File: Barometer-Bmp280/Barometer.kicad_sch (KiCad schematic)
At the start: 3 parts, among them U44 BMP280

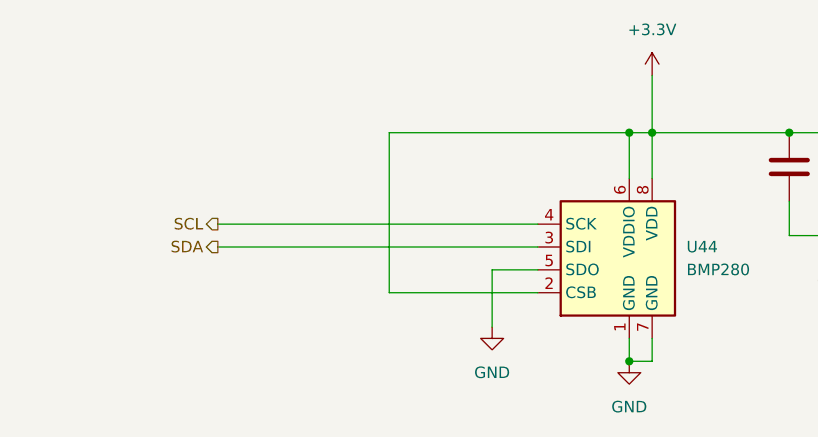
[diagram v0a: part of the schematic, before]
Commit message: Route sensors, IMU and radio board
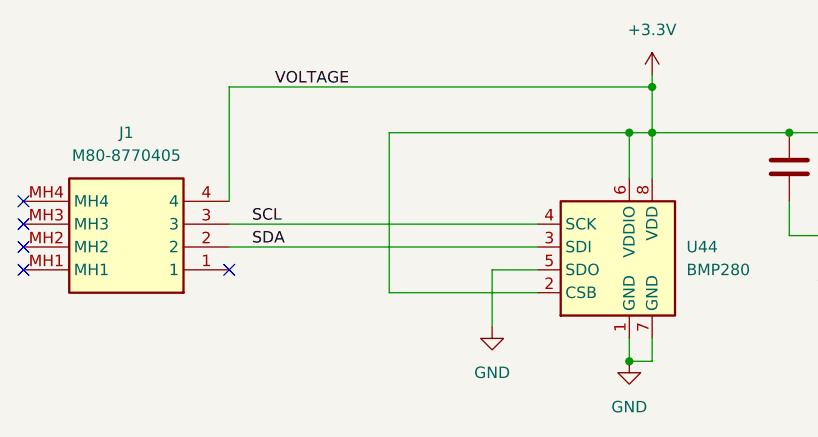
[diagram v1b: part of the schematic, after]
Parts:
- added J1: M80-8770405, M808770405, symbol M80-8770405:M80-8770405
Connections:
- net +3.3V: now also J1.4
- net SCL: now also J1.3
- net SDA: now also J1.2
- no-connect marks 0 -> 5
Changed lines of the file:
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@@
   (junction (at 173.99 96.52) (diameter 0) (color 0 0 0 0)
   )
+  (junction (at 158.75 91.44) (diameter 0) (color 0 0 0 0)
+  )
   (junction (at 179.07 107.95) (diameter 0) (color 0 0 0 0)
   )
@@
   (junction (at 158.75 96.52) (diameter 0) (color 0 0 0 0)
   )
-  (wire (pts (xy 110.49 109.22) (xy 146.05 109.22))
+  (no_connect (at 88.9 104.14))
+  (no_connect (at 111.76 111.76))
+  (no_connect (at 88.9 109.22))
+  (no_connect (at 88.9 106.68))
+  (no_connect (at 88.9 111.76))
+  (wire (pts (xy 111.76 91.44) (xy 158.75 91.44))
     (stroke (width 0) (type default))
   )
@@
     (stroke (width 0) (type default))
   )
+  (wire (pts (xy 111.76 109.22) (xy 146.05 109.22))
+    (stroke (width 0) (type default))
+  )
   (wire (pts (xy 179.07 107.95) (xy 186.69 107.95))
     (stroke (width 0) (type default))
@@
     (stroke (width 0) (type default))
   )
-  (wire (pts (xy 110.49 106.68) (xy 146.05 106.68))
-    (stroke (width 0) (type default))
-  )
   (wire (pts (xy 129.54 96.52) (xy 156.21 96.52))
     (stroke (width 0) (type default))
@@
     (stroke (width 0) (type default))
   )
+  (wire (pts (xy 111.76 106.68) (xy 146.05 106.68))
+    (stroke (width 0) (type default))
+  )
   (wire (pts (xy 186.69 107.95) (xy 186.69 104.14))
     (stroke (width 0) (type default))
@@
     (stroke (width 0) (type default))
   )
-  (wire (pts (xy 158.75 90.17) (xy 158.75 96.52))
+  (wire (pts (xy 158.75 90.17) (xy 158.75 91.44))
     (stroke (width 0) (type default))
   )
@@
     (stroke (width 0) (type default))
   )
-  (hierarchical_label "SDA" (shape output) (at 110.49 109.22 180) (fields_autoplaced)
-    (effects (font (size 1.27 1.27)) (justify right))
-  )
-  (hierarchical_label "SCL" (shape output) (at 110.49 106.68 180) (fields_autoplaced)
-    (effects (font (size 1.27 1.27)) (justify right))
+  (wire (pts (xy 158.75 91.44) (xy 158.75 96.52))
+    (stroke (width 0) (type default))
+  )
+  (wire (pts (xy 111.76 104.14) (xy 111.76 91.44))
+    (stroke (width 0) (type default))
+  )
+  (label "SCL" (at 114.3 106.68 0) (fields_autoplaced)
+    (effects (font (size 1.27 1.27)) (justify left bottom))
+  )
+  (label "SDA" (at 114.3 109.22 0) (fields_autoplaced)
+    (effects (font (size 1.27 1.27)) (justify left bottom))
+  )
+  (label "VOLTAGE" (at 116.84 91.44 0) (fields_autoplaced)
+    (effects (font (size 1.27 1.27)) (justify left bottom))
   )
   (symbol (lib_id "Device:C") (at 186.69 100.33 0) (unit 1)
@@
         )
       )
+    )
+  )
+  (symbol (lib_id "M80-8770405:M80-8770405") (at 111.76 111.76 180) (unit 1)
+    (in_bom yes) (on_board yes) (dnp no) (fields_autoplaced)
+    (property "Reference" "J1" (at 100.33 96.52 0)
+      (effects (font (size 1.27 1.27)))
+    )
+    (property "Value" "M80-8770405" (at 100.33 99.06 0)
+      (effects (font (size 1.27 1.27)))
+    )
+    (property "Footprint" "M808770405" (at 92.71 16.84 0)
+      (effects (font (size 1.27 1.27)) (justify left top) hide)
+    )
+    (property "Datasheet" "https://cdn.harwin.com/pdfs/M80-877.pdf" (at 92.71 -83.16 0)
+      (effects (font (size 1.27 1.27)) (justify left top) hide)
+    )
+    (property "Height" "5.56" (at 92.71 -283.16 0)
+      (effects (font (size 1.27 1.27)) (justify left top) hide)
+    )
+    (property "Manufacturer_Name" "Harwin" (at 92.71 -383.16 0)
+      (effects (font (size 1.27 1.27)) (justify left top) hide)
+    )
+    (property "Manufacturer_Part_Number" "M80-8770405" (at 92.71 -483.16 0)
+      (effects (font (size 1.27 1.27)) (justify left top) hide)
+    )
+    (property "Mouser Part Number" "855-M80-8770405" (at 92.71 -583.16 0)
+      (effects (font (size 1.27 1.27)) (justify left top) hide)
+    )
+    (property "Mouser Price/Stock" "https://www.mouser.co.uk/ProductDetail/Harwin/M80-8770405?qs=3tymCvhQ29ZPq83M%252Bf8kIA%3D%3D" (at 92.71 -683.16 0)
+      (effects (font (size 1.27 1.27)) (justify left top) hide)
+    )
+    (property "Arrow Part Number" "" (at 92.71 -783.16 0)
+      (effects (font (size 1.27 1.27)) (justify left top) hide)
+    )
+    (property "Arrow Price/Stock" "" (at 92.71 -883.16 0)
+      (effects (font (size 1.27 1.27)) (justify left top) hide)
+    )
+    (pin "1")
+    (pin "2")
+    (pin "3")
+    (pin "4")
+    (pin "MH1")
+    (pin "MH2")
+    (pin "MH3")
+    (pin "MH4")
+    (instances
+      (project "Barometer"
+        (path "/7f3991ce-16d8-4280-80b6-77a7b05059d0"
+          (reference "J1") (unit 1)
+        )
+      )

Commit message: Done with most of the boards
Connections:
- net GND: now also J1.1
- no-connect marks 5 -> 4
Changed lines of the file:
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@@
   (junction (at 156.21 121.92) (diameter 0) (color 0 0 0 0)
+  )
+  (junction (at 140.97 116.84) (diameter 0) (color 0 0 0 0)
   )
   (junction (at 158.75 96.52) (diameter 0) (color 0 0 0 0)
   )
   (no_connect (at 88.9 104.14))
-  (no_connect (at 111.76 111.76))
   (no_connect (at 88.9 109.22))
   (no_connect (at 88.9 106.68))
@@
   )
   (wire (pts (xy 173.99 96.52) (xy 186.69 96.52))
+    (stroke (width 0) (type default))
+  )
+  (wire (pts (xy 123.19 111.76) (xy 123.19 116.84))
     (stroke (width 0) (type default))
   )
@@
     (stroke (width 0) (type default))
   )
+  (wire (pts (xy 111.76 111.76) (xy 123.19 111.76))
+    (stroke (width 0) (type default))
+  )
   (wire (pts (xy 111.76 109.22) (xy 146.05 109.22))
     (stroke (width 0) (type default))
@@
     (stroke (width 0) (type default))
   )
+  (wire (pts (xy 123.19 116.84) (xy 140.97 116.84))
+    (stroke (width 0) (type default))
+  )
   (wire (pts (xy 129.54 114.3) (xy 129.54 96.52))
+    (stroke (width 0) (type default))
+  )
+  (wire (pts (xy 140.97 116.84) (xy 140.97 118.11))
     (stroke (width 0) (type default))
   )
@@
     (stroke (width 0) (type default))
   )
-  (wire (pts (xy 140.97 111.76) (xy 140.97 118.11))
+  (wire (pts (xy 140.97 111.76) (xy 140.97 116.84))
     (stroke (width 0) (type default))
   )

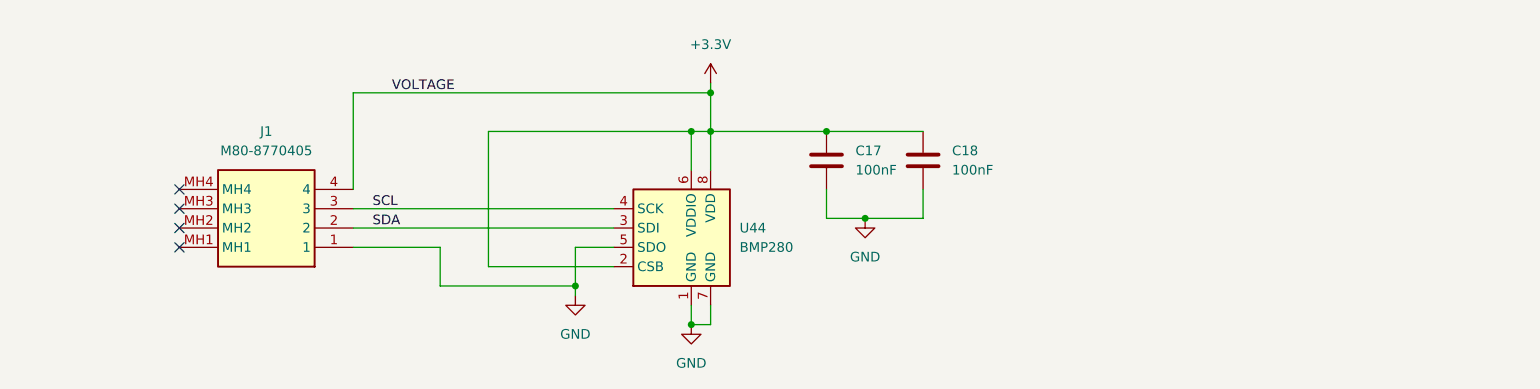
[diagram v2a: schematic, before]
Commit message: Fixed Accel, Barometer, FRAM, Inertia unit, and Magnetometer
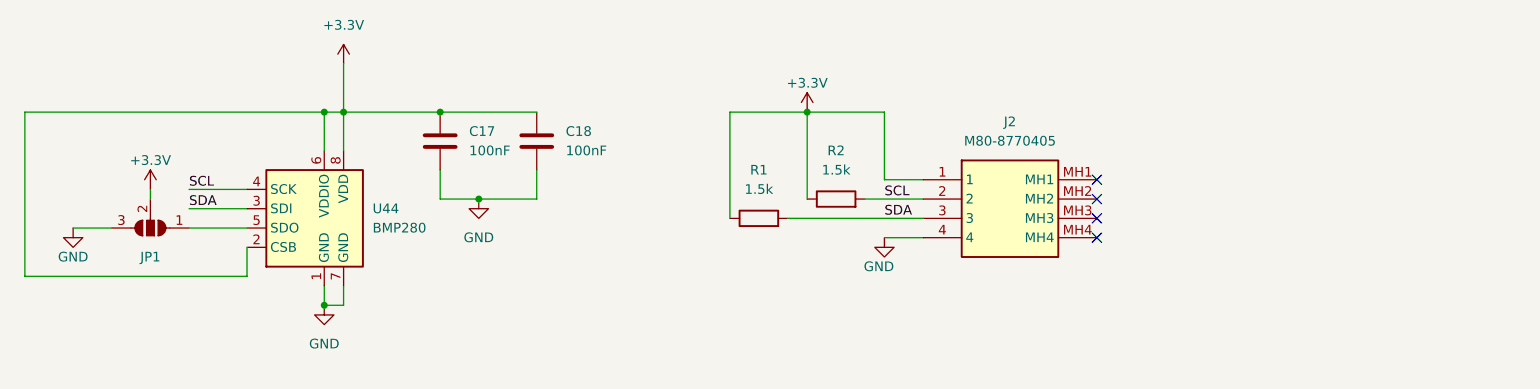
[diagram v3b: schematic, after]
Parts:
- removed J1: M80-8770405, M808770405, symbol M80-8770405:M80-8770405
- added J2: M80-8770405, M808770405, symbol M80-8770405:M80-8770405
- added JP1: SolderJumper_3_Open, Jumper:SolderJumper-3_P1.3mm_Open_RoundedPad1.0x1.5mm_NumberLabels, symbol Jumper:SolderJumper_3_Open
- added R1, R2: 1.5k, Resistor_SMD:R_0201_0603Metric_Pad0.64x0.40mm_HandSolder, symbol Device:R
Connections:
- net +3.3V: now also J2.1, JP1.2 (C), R1.1, R2.1
- net GND: now also J2.4, JP1.3 (B); no longer U44.5 (SDO)
- net SCL: now also J2.2, R2.2
- net SDA: now also J2.3, R1.2
- new net: JP1.1 (A), U44.5 (SDO)
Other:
- company: (none) -> USST Avionics
- title: (none) -> BMP280 Barometer
- moved on the sheet: C17, C18, U44

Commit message: Started fixing layouts
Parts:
- renumbered J2 to J1
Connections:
- net +3.3V: now also JP1.3 (B); no longer JP1.2 (C)
- net GND: now also JP1.1 (A); no longer JP1.3 (B)
- net at U44.5 (SDO): now also JP1.2 (C); no longer JP1.1 (A)
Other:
- moved on the sheet: JP1
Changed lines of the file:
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@@
     (stroke (width 0) (type default))
   )
-  (wire (pts (xy 97.79 115.57) (xy 68.58 115.57))
+  (wire (pts (xy 97.79 120.65) (xy 67.31 120.65))
     (stroke (width 0) (type default))
   )
@@
     (stroke (width 0) (type default))
   )
-  (wire (pts (xy 90.17 109.22) (xy 97.79 109.22))
+  (wire (pts (xy 85.09 114.3) (xy 85.09 115.57))
+    (stroke (width 0) (type default))
+  )
+  (wire (pts (xy 97.79 111.76) (xy 97.79 120.65))
+    (stroke (width 0) (type default))
+  )
+  (wire (pts (xy 85.09 102.87) (xy 85.09 104.14))
+    (stroke (width 0) (type default))
+  )
+  (wire (pts (xy 88.9 109.22) (xy 97.79 109.22))
     (stroke (width 0) (type default))
   )
@@
     (stroke (width 0) (type default))
   )
-  (wire (pts (xy 85.09 104.14) (xy 85.09 105.41))
-    (stroke (width 0) (type default))
-  )
   (wire (pts (xy 107.95 93.98) (xy 110.49 93.98))
     (stroke (width 0) (type default))
@@
     (stroke (width 0) (type default))
   )
-  (wire (pts (xy 97.79 115.57) (xy 97.79 111.76))
-    (stroke (width 0) (type default))
-  )
   (wire (pts (xy 168.91 107.95) (xy 186.69 107.95))
     (stroke (width 0) (type default))
@@
     (stroke (width 0) (type default))
   )
-  (wire (pts (xy 74.93 109.22) (xy 80.01 109.22))
-    (stroke (width 0) (type default))
-  )
   (wire (pts (xy 110.49 116.84) (xy 110.49 119.38))
     (stroke (width 0) (type default))
   )
-  (wire (pts (xy 68.58 93.98) (xy 107.95 93.98))
+  (wire (pts (xy 67.31 93.98) (xy 107.95 93.98))
     (stroke (width 0) (type default))
   )
@@
     (stroke (width 0) (type default))
   )
-  (wire (pts (xy 68.58 115.57) (xy 68.58 93.98))
+  (wire (pts (xy 67.31 120.65) (xy 67.31 93.98))
     (stroke (width 0) (type default))
   )
@@
     )
   )
-  (symbol (lib_id "Jumper:SolderJumper_3_Open") (at 85.09 109.22 180) (unit 1)
-    (in_bom yes) (on_board yes) (dnp no) (fields_autoplaced)
-    (property "Reference" "JP1" (at 85.09 113.03 0)
-      (effects (font (size 1.27 1.27)))
-    )
-    (property "Value" "SolderJumper_3_Open" (at 85.09 115.57 0)
+  (symbol (lib_id "Jumper:SolderJumper_3_Open") (at 85.09 109.22 90) (unit 1)
+    (in_bom yes) (on_board yes) (dnp no)
+    (property "Reference" "JP1" (at 88.9 115.57 90)
+      (effects (font (size 1.27 1.27)) (justify left))
+    )
+    (property "Value" "SolderJumper_3_Open" (at 78.74 109.22 0)
       (effects (font (size 1.27 1.27)) hide)
     )
@@
     )
   )
-  (symbol (lib_id "power:+3.3V") (at 85.09 104.14 0) (unit 1)
-    (in_bom yes) (on_board yes) (dnp no)
-    (property "Reference" "#PWR019" (at 85.09 107.95 0)
-      (effects (font (size 1.27 1.27)) hide)
-    )
-    (property "Value" "+3.3V" (at 85.09 100.33 0)
-      (effects (font (size 1.27 1.27)))
-    )
-    (property "Footprint" "" (at 85.09 104.14 0)
-      (effects (font (size 1.27 1.27)) hide)
-    )
-    (property "Datasheet" "" (at 85.09 104.14 0)
+  (symbol (lib_id "power:+3.3V") (at 85.09 102.87 0) (unit 1)
+    (in_bom yes) (on_board yes) (dnp no)
+    (property "Reference" "#PWR019" (at 85.09 106.68 0)
+      (effects (font (size 1.27 1.27)) hide)
+    )
+    (property "Value" "+3.3V" (at 85.09 99.06 0)
+      (effects (font (size 1.27 1.27)))
+    )
+    (property "Footprint" "" (at 85.09 102.87 0)
+      (effects (font (size 1.27 1.27)) hide)
+    )
+    (property "Datasheet" "" (at 85.09 102.87 0)
       (effects (font (size 1.27 1.27)) hide)
     )
@@
   (symbol (lib_id "M80-8770405:M80-8770405") (at 186.69 102.87 0) (unit 1)
     (in_bom yes) (on_board yes) (dnp no)
-    (property "Reference" "J2" (at 198.12 95.25 0)
+    (property "Reference" "J1" (at 198.12 95.25 0)
       (effects (font (size 1.27 1.27)))
     )
@@
       (project "Barometer"
         (path "/7f3991ce-16d8-4280-80b6-77a7b05059d0"
-          (reference "J2") (unit 1)
+          (reference "J1") (unit 1)
         )
       )
@@
     )
   )
-  (symbol (lib_id "power:GND") (at 74.93 109.22 0) (unit 1)
-    (in_bom yes) (on_board yes) (dnp no)
-    (property "Reference" "#PWR03" (at 74.93 115.57 0)
-      (effects (font (size 1.27 1.27)) hide)
-    )
-    (property "Value" "GND" (at 74.93 113.03 0)
-      (effects (font (size 1.27 1.27)))
-    )
-    (property "Footprint" "" (at 74.93 109.22 0)
-      (effects (font (size 1.27 1.27)) hide)
-    )
-    (property "Datasheet" "" (at 74.93 109.22 0)
-      (effects (font (size 1.27 1.27)) hide)
-    )
+  (symbol (lib_id "power:GND") (at 85.09 115.57 0) (unit 1)
+    (in_bom yes) (on_board yes) (dnp no)
+    (property "Reference" "#PWR03" (at 85.09 121.92 0)
+      (effects (font (size 1.27 1.27)) hide)
+    )
+    (property "Value" "GND" (at 85.09 119.38 0)
+      (effects (font (size 1.27 1.27)))
+    )
+    (property "Footprint" "" (at 85.09 115.57 0)
+      (effects (font (size 1.27 1.27)) hide)
+    )
+    (property "Datasheet" "" (at 85.09 115.57 0)
+      (effects (font (size 1.27 1.27)) hide)
+    )

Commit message: LC24 PCBs
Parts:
- removed J1: M80-8770405, M808770405, symbol M80-8770405:M80-8770405
- added H1, H2, H3, H4: MountingHole_Pad, Mounting_Wuerth:Mounting_Wuerth_WA-SMSI-M1.6_H1mm_9774010633, symbol Mechanical:MountingHole_Pad
- added J2: M80-8770422, Harwin-M80-8770422:CONN_M80-87704_HRW, symbol Harwin-M80-8770422:M80-8770422
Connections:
- net +3.3V: now also J2.1
- net GND: now also H1.1, H2.1, H3.1, H4.1, J2.4
- net SCL: now also J2.2
- net SDA: now also J2.3
- no-connect marks 4 -> 0
